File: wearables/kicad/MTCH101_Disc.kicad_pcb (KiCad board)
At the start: 2 copper layers, 13 parts, among them U1 MTCH101

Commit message: more exploration
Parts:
- removed W1: TEST_MTI, Measurement_Points:Measurement_Point_Round-SMD-Pad_Small
- added P1: SNS, Pin_Headers:Pin_Header_Straight_2x02, F.Cu at (123.2, 94.5)
- added W2: TEST_GND, Measurement_Points:Measurement_Point_Round-TH_Big, F.Cu at (124.5, 105.9)
- added W5: TEST_VDD, Measurement_Points:Measurement_Point_Round-TH_Big, F.Cu at (124.5, 85.6)
- D1: footprint LEDs:LED_0603 -> LEDs:LED_1206
- W3, W4: footprint Measurement_Points:Measurement_Point_Round-SMD-Pad_Small -> Mounting_Holes:MountingHole_2.2mm_M2_Pad
- moved R4 39.6 mm to (118.7, 95.8), turned to 90 degrees
- moved U1 38.4 mm to (124.5, 101.5)
- moved R5 35.5 mm to (128.3, 95.8), turned to 90 degrees
- moved R1 29.5 mm to (120.7, 93.9), turned to 270 degrees
- moved R6 27.1 mm to (125.7, 90.7)
- moved W3 25.0 mm to (114.3, 95.8)
- moved D1 24.2 mm to (123.2, 90.7), turned to 180 degrees
- moved R2 22.5 mm to (120.7, 97.7), turned to 270 degrees
- moved W6 21.7 mm to (127.6, 98.9)
- moved C1 20.3 mm to (130.0, 95.8), turned to 270 degrees
- moved R3 15.0 mm to (124.5, 98.9)
- moved W4 10.7 mm to (134.6, 95.8)
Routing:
- net /out: track 0.00 -> 11.8 mm
- net VDD: track 0.00 -> 11.6 mm
- net /pm: track 0.00 -> 5.42 mm
- added copper zone on B.Cu, net /sns
- added copper zone on B.Cu, net GND
- added copper zone on F.Cu, net GND
- added copper zone on B.Cu, net VDD
- added copper zone on F.Cu, net VDD
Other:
- board outline added: 25.4 x 25.4 mm

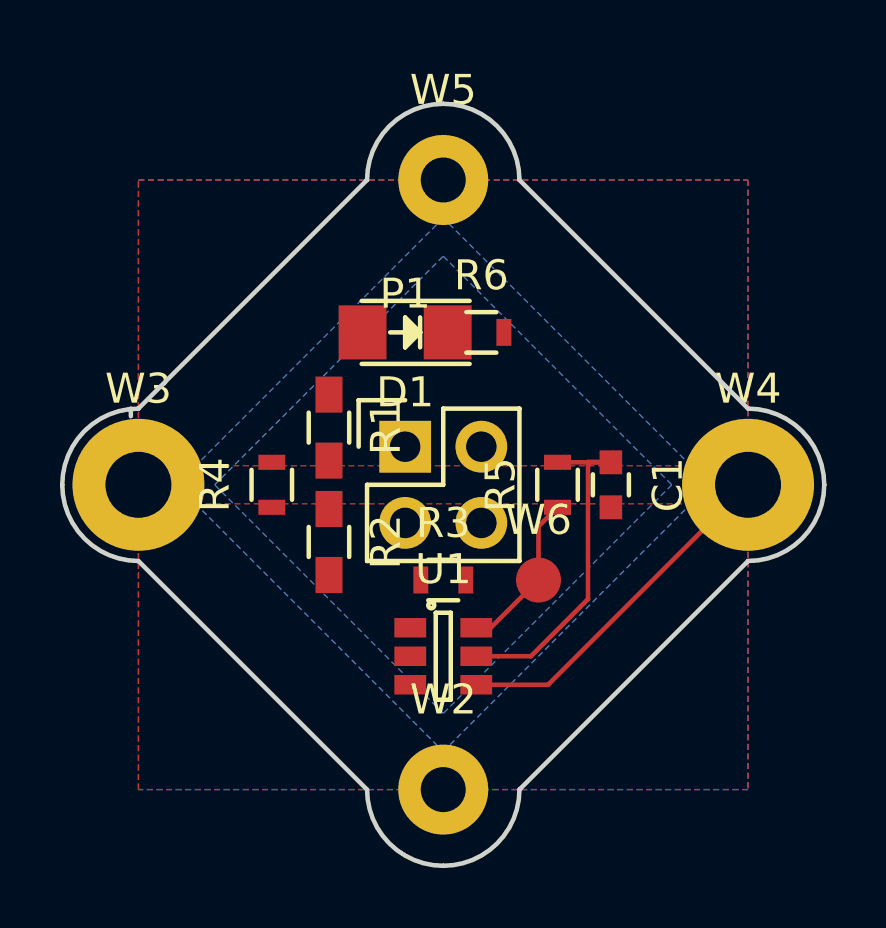
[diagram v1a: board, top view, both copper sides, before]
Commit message: Creating button connector library
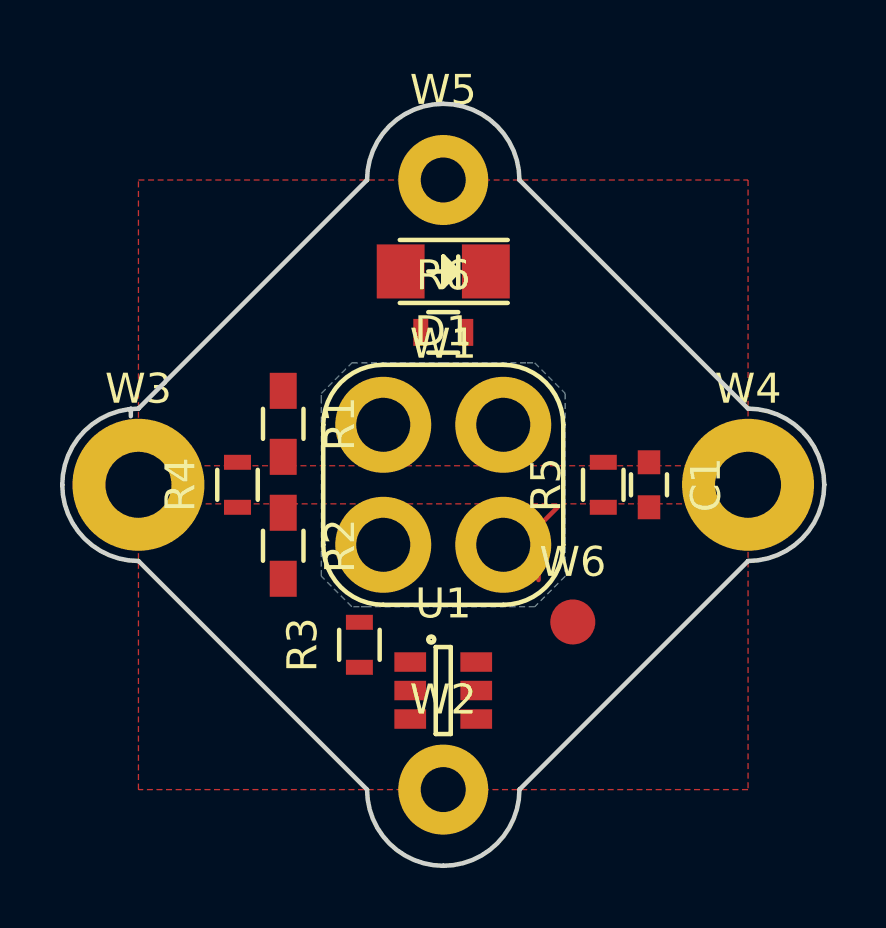
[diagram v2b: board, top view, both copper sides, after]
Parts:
- removed P1: SNS, Pin_Headers:Pin_Header_Straight_2x02
- added W1: sns, buttons:sew_2x2, F.Cu at (124.5, 95.8)
- R2: value OPEN -> 100k
- moved R3 3.53 mm to (121.7, 101.1), turned to 90 degrees
- moved D1 2.40 mm to (124.5, 88.6)
- moved W6 1.81 mm to (128.8, 100.3)
- moved R2 1.53 mm to (119.1, 97.8)
- moved R1 1.53 mm to (119.1, 93.7)
- moved R5 1.52 mm to (129.8, 95.8)
- moved C1 1.27 mm to (131.3, 95.8)
- moved R6 1.27 mm to (124.5, 90.7)
- moved R4 1.14 mm to (117.6, 95.8)
- moved U1 1.14 mm to (124.5, 102.6)
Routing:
- net /out: track 11.8 -> 0.00 mm
- net VDD: track 11.6 -> 0.00 mm
- net /pm: track 5.42 -> 0.00 mm
- net /sns: track 0.00 -> 2.69 mm
- removed copper zone on B.Cu, net GND
- removed copper zone on B.Cu, net VDD
